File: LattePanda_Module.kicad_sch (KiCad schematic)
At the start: 12 parts, among them J1 Conn_01x03_Pin

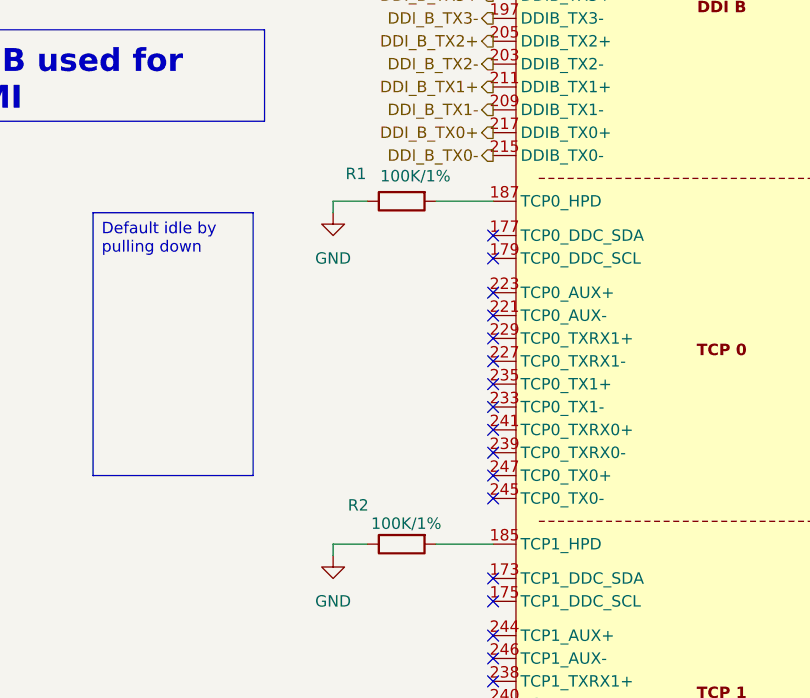
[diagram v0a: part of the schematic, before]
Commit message: added USB-C
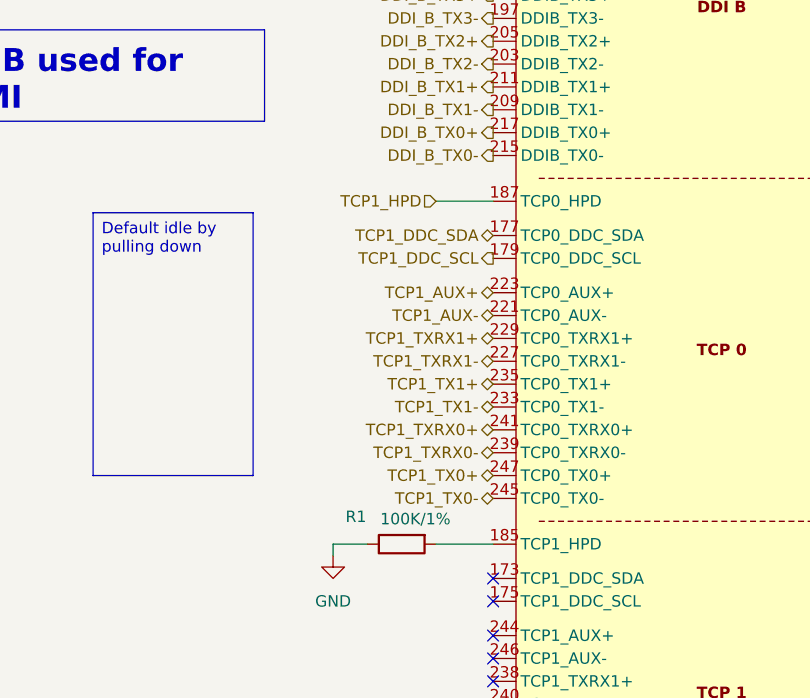
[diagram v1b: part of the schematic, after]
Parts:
- removed R2: 100K/1%, A_DFRobot:R_0603_1608Metric, symbol Device:R
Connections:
- net at A1.185 (TCP1_HPD): now also R1.2
- net TCP1_HPD: now reaches A1.187 (TCP0_HPD)
- net TCP1_HPD: no longer R1.2
- net TCP1_DDC_SDA: now reaches A1.177 (TCP0_DDC_SDA)
- net TCP1_DDC_SCL: now reaches A1.179 (TCP0_DDC_SCL)
- net TCP1_AUX-: now reaches A1.221 (TCP0_AUX-)
- net TCP1_AUX+: now reaches A1.223 (TCP0_AUX+)
- net TCP1_TXRX1-: now reaches A1.227 (TCP0_TXRX1-)
- net TCP1_TXRX1+: now reaches A1.229 (TCP0_TXRX1+)
- net TCP1_TX1-: now reaches A1.233 (TCP0_TX1-)
- net TCP1_TX1+: now reaches A1.235 (TCP0_TX1+)
- net TCP1_TXRX0-: now reaches A1.239 (TCP0_TXRX0-)
- net TCP1_TXRX0+: now reaches A1.241 (TCP0_TXRX0+)
- net TCP1_TX0-: now reaches A1.245 (TCP0_TX0-)
- net TCP1_TX0+: now reaches A1.247 (TCP0_TX0+)
- no-connect marks 73 -> 61

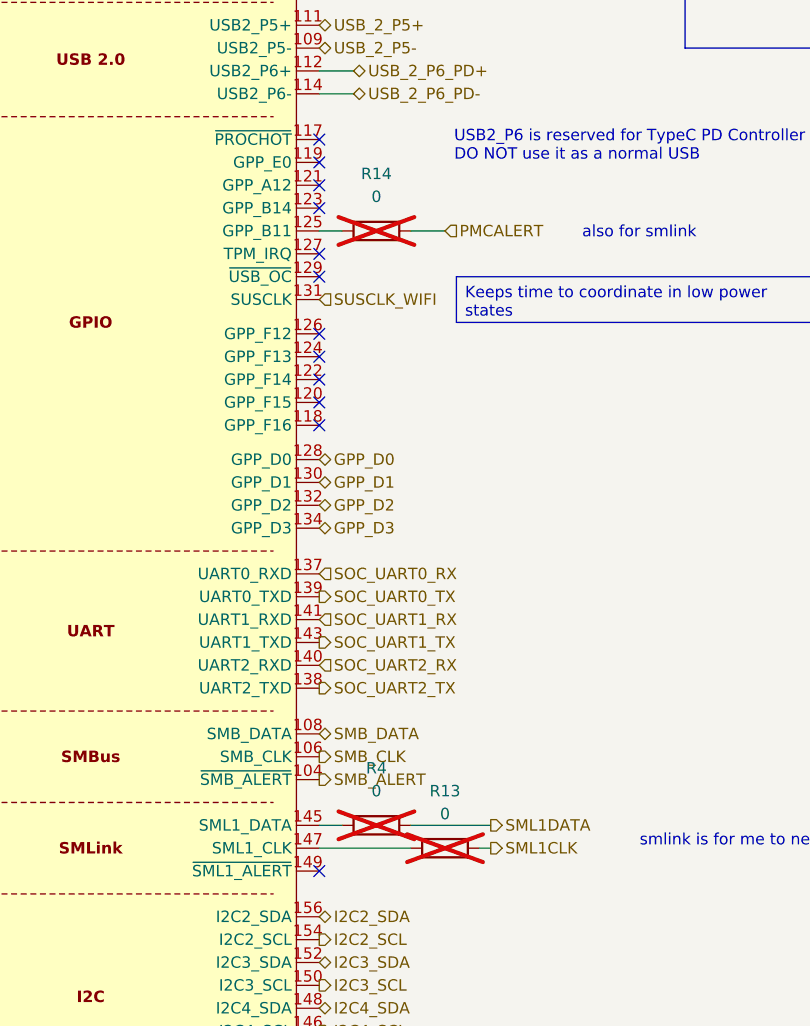
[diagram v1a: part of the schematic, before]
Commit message: enable sml
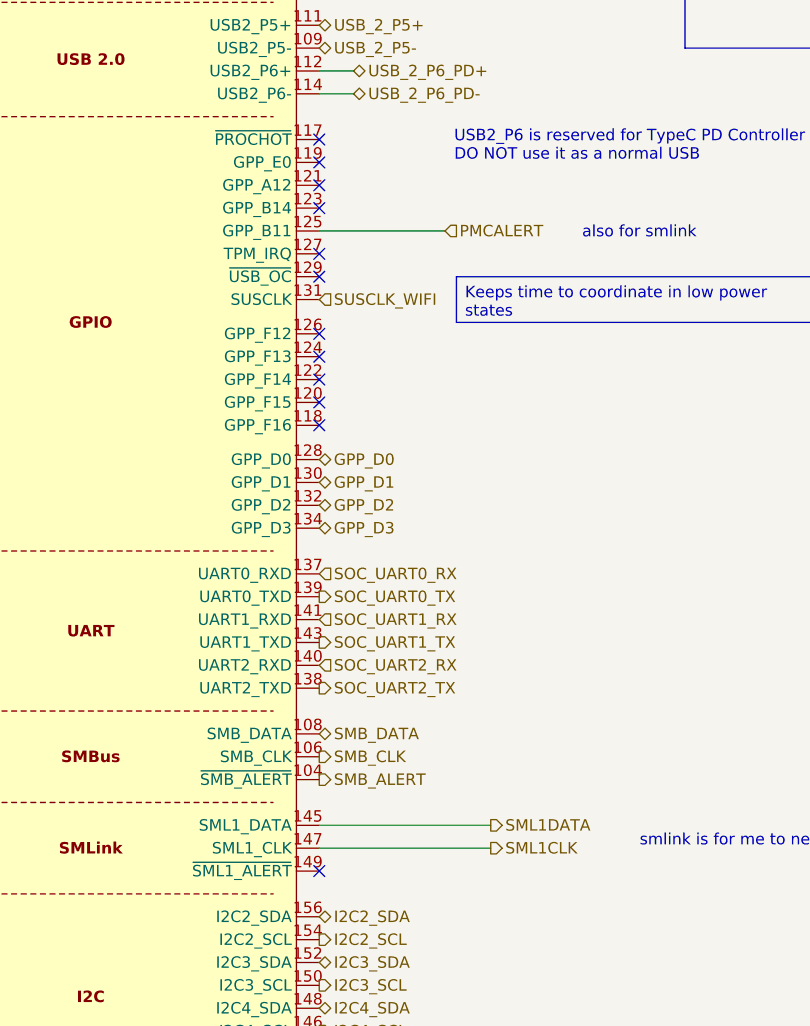
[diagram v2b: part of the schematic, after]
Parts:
- removed R13, R14, R4: 0, A_DFRobot:R_0603_1608Metric, symbol Device:R
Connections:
- net PMCALERT: now also A1.125 (GPP_B11)
- net SML1CLK: now also A1.147 (SML1_CLK)
- net SML1DATA: now also A1.145 (SML1_DATA)

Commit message: last push before editing with the grid view (gonna break everything)
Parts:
- A1: MPN (none) -> ASAA821-EASB0-7H
- BT1: MPN (none) -> BS-12-B3AA003
- H12, H13, J1, TP1: now left out of the parts list
- R1: value 100K/1% -> 100K; MPN (none) -> 0603L005/6AR
- R3: value 1K/1% -> 1K; MPN (none) -> 0603L005/6AR
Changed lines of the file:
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@@
 		(body_style 1)
 		(exclude_from_sim no)
-		(in_bom yes)
+		(in_bom no)
 		(on_board yes)
 		(in_pos_files yes)
@@
 		(body_style 1)
 		(exclude_from_sim no)
-		(in_bom yes)
+		(in_bom no)
 		(on_board yes)
 		(in_pos_files yes)
@@
 		(body_style 1)
 		(exclude_from_sim no)
-		(in_bom yes)
+		(in_bom no)
 		(on_board yes)
 		(in_pos_files yes)
@@
 			)
 		)
-		(property "Value" "100K/1%"
+		(property "Value" "100K"
 			(at 235.204 288.036 90)
 			(show_name no)
@@
 			)
 		)
-		(property "Description" "Resistor"
+		(property "Description" "1%"
 			(at 233.68 290.83 0)
 			(hide yes)
@@
 		(property "SCH_Show_Footprint" "R0805"
 			(at 233.68 290.83 0)
+			(hide yes)
+			(show_name no)
+			(do_not_autoplace no)
+			(effects
+				(font
+					(size 1.27 1.27)
+				)
+			)
+		)
+		(property "MPN" "0603L005/6AR"
+			(at 233.68 290.83 90)
 			(hide yes)
 			(show_name no)
@@
 		(body_style 1)
 		(exclude_from_sim no)
-		(in_bom yes)
+		(in_bom no)
 		(on_board yes)
 		(in_pos_files yes)
@@
 			)
 		)
+		(property "MPN" "ASAA821-EASB0-7H"
+			(at 284.48 196.85 0)
+			(hide yes)
+			(show_name no)
+			(do_not_autoplace no)
+			(effects
+				(font
+					(size 1.27 1.27)
+				)
+			)
+		)
 		(pin "210"
 		)
@@
 			)
 		)
-		(property "Value" "1K/1%"
+		(property "Value" "1K"
 			(at 300.99 57.15 90)
 			(show_name no)
@@
 			)
 		)
-		(property "Description" "Resistor"
+		(property "Description" "1%"
 			(at 298.45 54.61 0)
 			(hide yes)
@@
 		(property "SCH_Show_Footprint" "R0805"
 			(at 298.45 54.61 0)
+			(hide yes)
+			(show_name no)
+			(do_not_autoplace no)
+			(effects
+				(font
+					(size 1.27 1.27)
+				)
+			)
+		)
+		(property "MPN" "0603L005/6AR"
+			(at 298.45 54.61 90)
 			(hide yes)
 			(show_name no)
@@
 		(body_style 1)
 		(exclude_from_sim no)
-		(in_bom yes)
+		(in_bom no)
 		(on_board yes)
 		(in_pos_files yes)
@@
 		(body_style 1)
 		(exclude_from_sim no)
-		(in_bom yes)
+		(in_bom no)
 		(on_board yes)
 		(in_pos_files yes)
@@
 			(hide yes)
 			(show_name no)
+			(do_not_autoplace no)
+			(effects
+				(font
+					(size 1.27 1.27)
+				)
+			)
+		)
+		(property "MPN" "BS-12-B3AA003"
+			(at 309.88 54.61 90)
+			(hide yes)
+			(show_name no)

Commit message: added MPN to all parts by hand :'(
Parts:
- R1: footprint A_DFRobot:R_0603_1608Metric -> A_DFRobot:R_0402; DF_Comment 0603贴片自恢复保险丝0.05A-6V_0603L005-6AR -> (none); MPN 0603L005/6AR -> RCS0402100KFKED; SCH_Show_Footprint R0805 -> (none)
- R3: footprint A_DFRobot:R_0603_1608Metric -> A_DFRobot:R_0402; Buy_Link https://item.szlcsc.com/8530937.html -> (none); DF_Comment 0603贴片自恢复保险丝0.05A-6V_0603L005-6AR -> (none); MPN 0603L005/6AR -> RCS04021K00JNED; SCH_Show_Footprint R0805 -> (none)
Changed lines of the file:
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@@
 			)
 		)
-		(property "Footprint" "A_DFRobot:R_0603_1608Metric"
+		(property "Footprint" "A_DFRobot:R_0402"
 			(at 233.68 289.052 90)
 			(hide yes)
@@
 			)
 		)
-		(property "DF_Comment" "0603贴片自恢复保险丝0.05A-6V_0603L005-6AR"
+		(property "DF_Comment" ""
 			(at 233.68 290.83 0)
 			(hide yes)
@@
 			)
 		)
-		(property "SCH_Show_Footprint" "R0805"
+		(property "SCH_Show_Footprint" ""
 			(at 233.68 290.83 0)
 			(hide yes)
@@
 			)
 		)
-		(property "MPN" "0603L005/6AR"
+		(property "MPN" "RCS0402100KFKED"
 			(at 233.68 290.83 90)
 			(hide yes)
@@
 			(project "microcyber"
 				(path "/7ac319af-771c-4997-a005-b73a4a9b44ab/64b35e3f-e07a-4023-bcd4-186bab824450"
+					(reference "R1")
+					(unit 1)
+				)
+				(path "/7ac319af-771c-4997-a005-b73a4a9b44ab/bf9d2aec-36d6-402d-b3de-6cf70c51ac31"
 					(reference "R1")
 					(unit 1)
@@
 			)
 		)
-		(property "Footprint" "A_DFRobot:R_0603_1608Metric"
+		(property "Footprint" "A_DFRobot:R_0402"
 			(at 298.45 52.832 90)
 			(hide yes)
@@
 			)
 		)
-		(property "Buy_Link" "https://item.szlcsc.com/8530937.html"
+		(property "Buy_Link" ""
 			(at 298.45 54.61 0)
 			(hide yes)
@@
 			)
 		)
-		(property "DF_Comment" "0603贴片自恢复保险丝0.05A-6V_0603L005-6AR"
+		(property "DF_Comment" ""
 			(at 298.45 54.61 0)
 			(hide yes)
@@
 			)
 		)
-		(property "SCH_Show_Footprint" "R0805"
+		(property "SCH_Show_Footprint" ""
 			(at 298.45 54.61 0)
 			(hide yes)
@@
 			)
 		)
-		(property "MPN" "0603L005/6AR"
+		(property "MPN" "RCS04021K00JNED"
 			(at 298.45 54.61 90)
 			(hide yes)
